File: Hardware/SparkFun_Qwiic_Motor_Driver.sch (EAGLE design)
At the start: 42 parts, among them U1 CY8C4245LQI-483, U2 DRV8835

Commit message: v01
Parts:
- LOGO3: value SFE_LOGO_NAME_FLAME.1_INCH -> SFE_LOGO_NAME.1_INCH; device SparkFun-Aesthetics:SFE_LOGO_NAME_FLAME.1_INCH -> SparkFun-Aesthetics:SFE_LOGO_NAME.1_INCH
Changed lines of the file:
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@@
 <part name="GND25" library="SparkFun-Aesthetics" deviceset="GND" device=""/>
 <part name="LOGO2" library="SparkFun-Aesthetics" deviceset="OSHW-LOGO" device="MINI"/>
-<part name="LOGO3" library="SparkFun-Aesthetics" deviceset="SFE_LOGO_NAME_FLAME" device=".1_INCH"/>
+<part name="LOGO3" library="SparkFun-Aesthetics" deviceset="SFE_LOGO_NAME" device=".1_INCH"/>
 <part name="R6" library="SparkFun-Resistors" deviceset="470OHM" device="-0603-1/10W-1%" value="470"/>
 <part name="GND26" library="SparkFun-Aesthetics" deviceset="GND" device=""/>

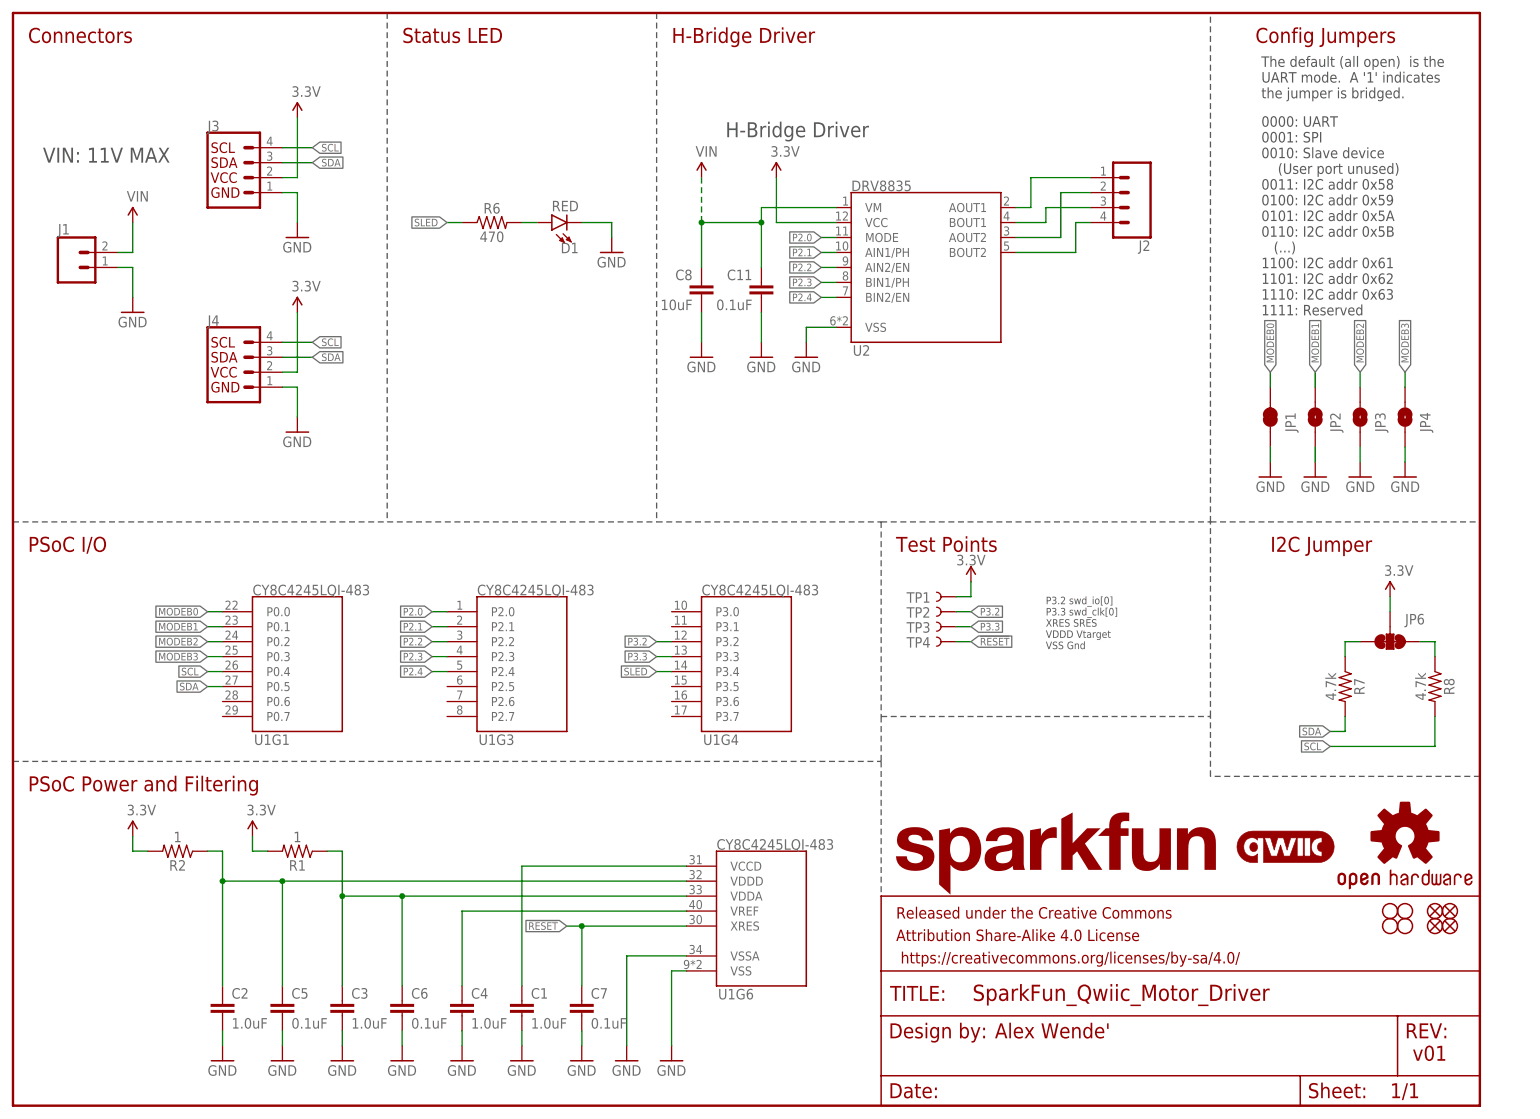
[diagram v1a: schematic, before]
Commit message: v01 Design Review Changes
- Added I2C test points
- Moved motor connector symbol to connection section
- Changed status LED to blue
- Adjusted VIN trace width
- Added SFE flame to top side of board
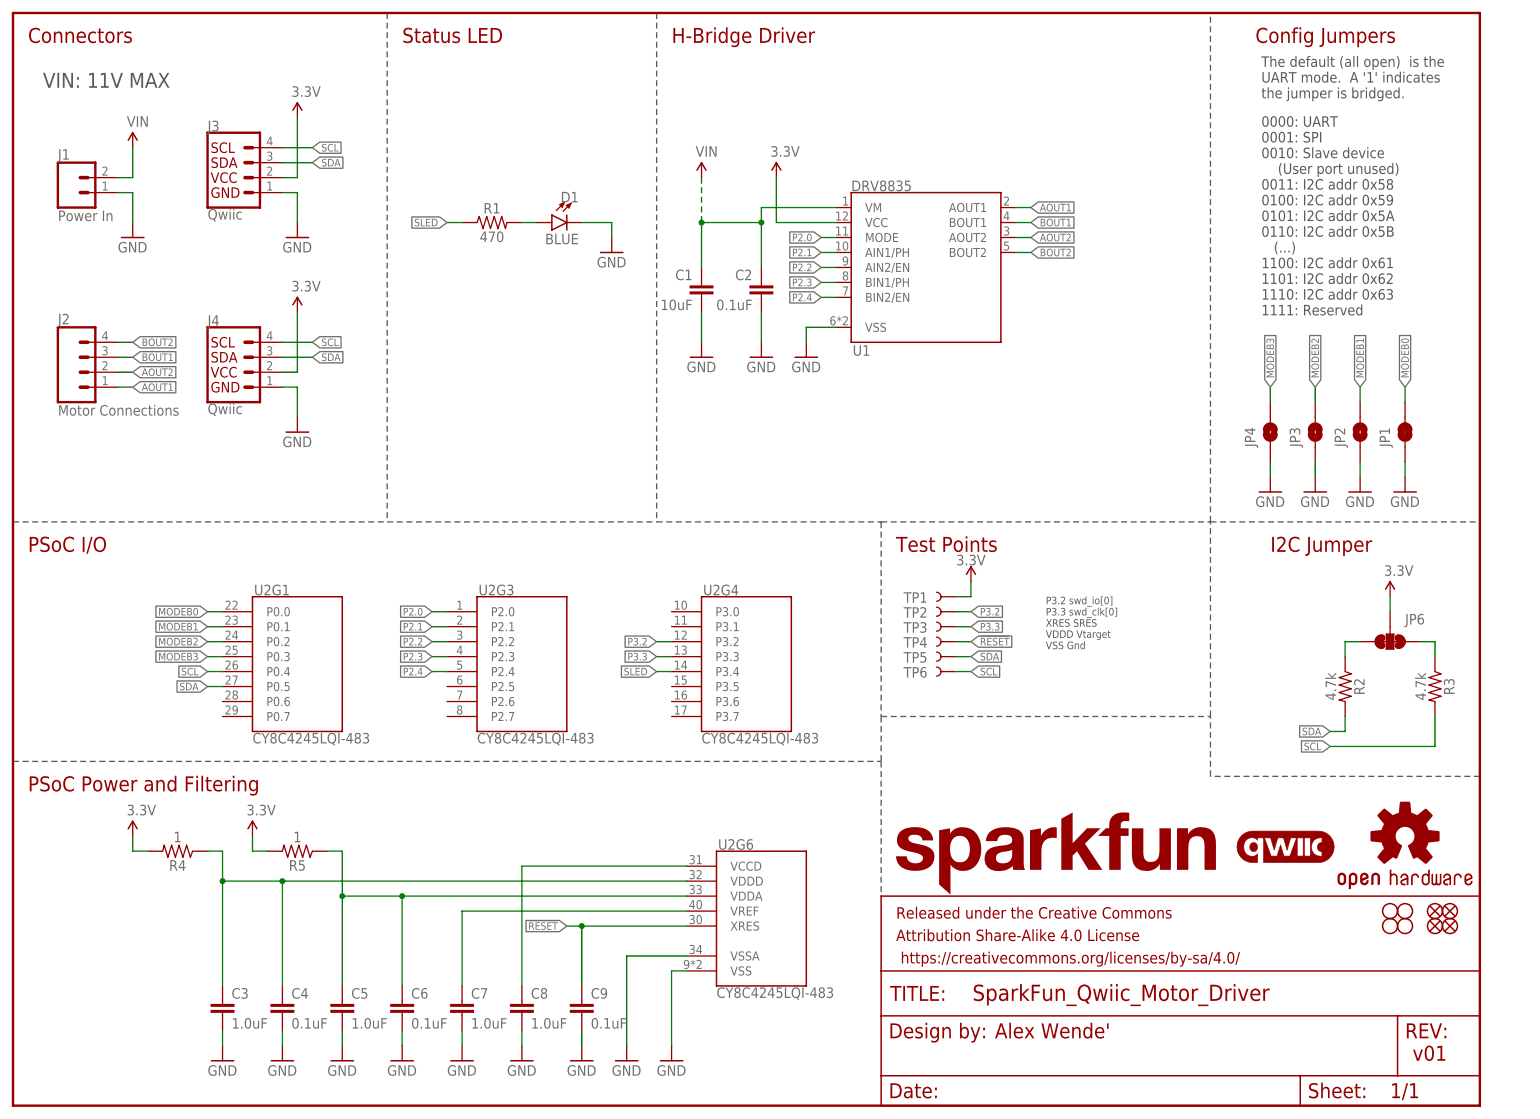
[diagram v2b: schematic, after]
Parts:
- removed C11: 0.1uF, SparkFun-Capacitors:0.1UF-0402-16V-10%
- removed R6: 470, SparkFun-Resistors:470OHM-0603-1/10W-1%
- removed R7: 4.7k, SparkFun-Resistors:4.7KOHM-0603-1/10W-1%
- added C9: 0.1uF, SparkFun-Capacitors:0.1UF-0402-16V-10%
- added R4, R5: 1, SparkFun-Resistors:1OHM-0603-1/10W-1%
- added TP5, TP6: TEST-POINTTP_15TH_THRU, SparkFun-Connectors:TEST-POINTTP_15TH_THRU
- C1: value 1.0uF -> 10uF; device SparkFun-Capacitors:1.0UF-0402-16V-10% -> SparkFun-Capacitors:10UF-0805-25V-10%
- C2, C4: value 1.0uF -> 0.1uF; device SparkFun-Capacitors:1.0UF-0402-16V-10% -> SparkFun-Capacitors:0.1UF-0402-16V-10%
- C5, C7: value 0.1uF -> 1.0uF; device SparkFun-Capacitors:0.1UF-0402-16V-10% -> SparkFun-Capacitors:1.0UF-0402-16V-10%
- C8: value 10uF -> 1.0uF; device SparkFun-Capacitors:10UF-0805-25V-10% -> SparkFun-Capacitors:1.0UF-0402-16V-10%
- D1: value RED -> BLUE; device SparkFun-LED:LED-RED0603 -> SparkFun-LED:LED-BLUE0603
- J1: value (none) -> Power In
- J2: value (none) -> Motor Connections
- J3, J4: value (none) -> Qwiic
- R1: value 1 -> 470; device SparkFun-Resistors:1OHM-0603-1/10W-1% -> SparkFun-Resistors:470OHM-0603-1/10W-1%
- R2: value 1 -> 4.7k; device SparkFun-Resistors:1OHM-0603-1/10W-1% -> SparkFun-Resistors:4.7KOHM-0603-1/10W-1%
- TP1, TP4: value RESET -> TEST-POINTTP_15TH_THRU
- TP2: value SWD_IO -> TEST-POINTTP_15TH_THRU
- TP3: value SWD_CLK -> TEST-POINTTP_15TH_THRU
- U1: value CY8C4245LQI-483 -> DRV8835; device PSOC4TempLib:CY8C4245LQI -> SparkFun-IC-Special-Function:DRV883X; PROD_ID (none) -> IC-13342
- U2: value DRV8835 -> CY8C4245LQI-483; device PSOC4TempLib:DRV883X -> SparkFun-IC-Microcontroller:PSOC4_4200_40QFN; PROD_ID IC-13342 -> (none)
- renumbered R8 to R3
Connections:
- net !RESET: now also C9.1, U2G6.XRES; no longer C7.1, U1G6.XRES
- net 3.3V: now also R4.2, R5.2, U1.VCC; no longer R1.2, R2.2, U2.VCC
- net AOUT1: now also U1.AOUT1; no longer U2.AOUT1
- net AOUT2: now also U1.AOUT2; no longer U2.AOUT2
- net BOUT1: now also U1.BOUT1; no longer U2.BOUT1
- net BOUT2: now also U1.BOUT2; no longer U2.BOUT2
- net GND: now also C9.2, U1.VSS, U2G6.VSS, U2G6.VSSA; no longer C11.2, U1G6.VSS, U1G6.VSSA, U2.VSS
- net MODEB0: now also U2G1.P0.0; no longer U1G1.P0.0
- net MODEB1: now also U2G1.P0.1; no longer U1G1.P0.1
- net MODEB2: now also U2G1.P0.2; no longer U1G1.P0.2
- net MODEB3: now also U2G1.P0.3; no longer U1G1.P0.3
- net N$1: now also C8.1, U2G6.VCCD; no longer C1.1, U1G6.VCCD
- net N$10: now also R1.2; no longer R6.2
- net N$12: now also R2.1; no longer R7.1
- net N$3: now also C5.1, R5.1, U2G6.VDDA; no longer C3.1, R1.1, U1G6.VDDA
- net N$4: now also C7.1, U2G6.VREF; no longer C4.1, U1G6.VREF
- net P2.0: now also U1.MODE, U2G3.P2.0; no longer U1G3.P2.0, U2.MODE
- net P2.1: now also U1.AIN1/PH, U2G3.P2.1; no longer U1G3.P2.1, U2.AIN1/PH
- net P2.2: now also U1.AIN2/EN, U2G3.P2.2; no longer U1G3.P2.2, U2.AIN2/EN
- net P2.3: now also U1.BIN1/PH, U2G3.P2.3; no longer U1G3.P2.3, U2.BIN1/PH
- net P2.4: now also U1.BIN2/EN, U2G3.P2.4; no longer U1G3.P2.4, U2.BIN2/EN
- net P3.2: now also U2G4.P3.2; no longer U1G4.P3.2
- net P3.3: now also U2G4.P3.3; no longer U1G4.P3.3
- net SCL: now also TP6.1, U2G1.P0.4; no longer U1G1.P0.4
- net SDA: now also R2.2, TP5.1, U2G1.P0.5; no longer R7.2, U1G1.P0.5
- net SLED: now also R1.1, U2G4.P3.4; no longer R6.1, U1G4.P3.4
- net VDDD: now also C3.1, C4.1, R4.1, U2G6.VDDD; no longer C2.1, C5.1, R2.1, U1G6.VDDD
- net VIN: now also C1.1, C2.1, U1.VM; no longer C11.1, C8.1, U2.VM
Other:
- moved on the sheet: C1, C2, C3, C4, C5, C7, C8, D1, J1, J2, JP1, JP2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

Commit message: v10
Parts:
- JP1: device SparkFun-Jumpers:JUMPER-SMT_2_NC_TRACE_NO-SILK -> SparkFun-Jumpers:JUMPER-SMT_2_NO_NO-SILK
- JP4: device SparkFun-Jumpers:JUMPER-SMT_2_NO_NO-SILK -> SparkFun-Jumpers:JUMPER-SMT_2_NC_TRACE_NO-SILK
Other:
- note added: "Alex Wende"
- note added: "P3.2 swd_io[0] P3.3 swd_clk[0]"
- note added: "v10"
- note removed: "Alex Wende'"
- note removed: "P3.2 swd_io[0] P3.3 swd_clk[0] XRES SRES VDDD Vtarget VSS Gnd"
- note removed: "v01"
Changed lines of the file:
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@@
 <part name="C2" library="SparkFun-Capacitors" deviceset="0.1UF" device="-0402-16V-10%" value="0.1uF"/>
 <part name="GND23" library="SparkFun-Aesthetics" deviceset="GND" device=""/>
-<part name="JP4" library="SparkFun-Jumpers" deviceset="JUMPER-SMT_2_NO" device="_NO-SILK" value="JUMPER-PAD-2"/>
+<part name="JP4" library="SparkFun-Jumpers" deviceset="JUMPER-SMT_2_NC_TRACE" device="_NO-SILK" value="JUMPER-PAD-2"/>
 <part name="JP3" library="SparkFun-Jumpers" deviceset="JUMPER-SMT_2_NO" device="_NO-SILK" value="JUMPER-PAD-2"/>
 <part name="JP2" library="SparkFun-Jumpers" deviceset="JUMPER-SMT_2_NO" device="_NO-SILK" value="JUMPER-PAD-2"/>
-<part name="JP1" library="SparkFun-Jumpers" deviceset="JUMPER-SMT_2_NC_TRACE" device="_NO-SILK" value="JUMPER-PAD-2"/>
+<part name="JP1" library="SparkFun-Jumpers" deviceset="JUMPER-SMT_2_NO" device="_NO-SILK" value="JUMPER-PAD-2"/>
 <part name="GND25" library="SparkFun-Aesthetics" deviceset="GND" device=""/>
 <part name="LOGO2" library="SparkFun-Aesthetics" deviceset="OSHW-LOGO" device="MINI"/>
@@
 <text x="2.54" y="53.34" size="2.54" layer="94" font="vector" ratio="15">PSoC Power and Filtering</text>
 <text x="210.82" y="180.34" size="2.54" layer="94" font="vector" ratio="15">Config Jumpers</text>
-<text x="166.624" y="11.43" size="2.54" layer="94" font="vector">Alex Wende'</text>
+<text x="166.624" y="11.43" size="2.54" layer="94" font="vector">Alex Wende</text>
 <text x="2.54" y="93.98" size="2.54" layer="94" font="vector" ratio="15">PSoC I/O</text>
-<text x="237.49" y="7.62" size="2.54" layer="94" font="vector">v01</text>
+<text x="237.49" y="7.62" size="2.54" layer="94" font="vector">v10</text>
 <text x="175.26" y="86.36" size="1.27" layer="97" font="vector" rot="MR180">P3.2 swd_io[0]
 P3.3 swd_clk[0]
-XRES SRES
-VDDD Vtarget
-VSS Gnd</text>
+</text>
 <text x="211.836" y="167.894" size="1.778" layer="97" font="vector" align="top-left">0000: UART
 0001: SPI

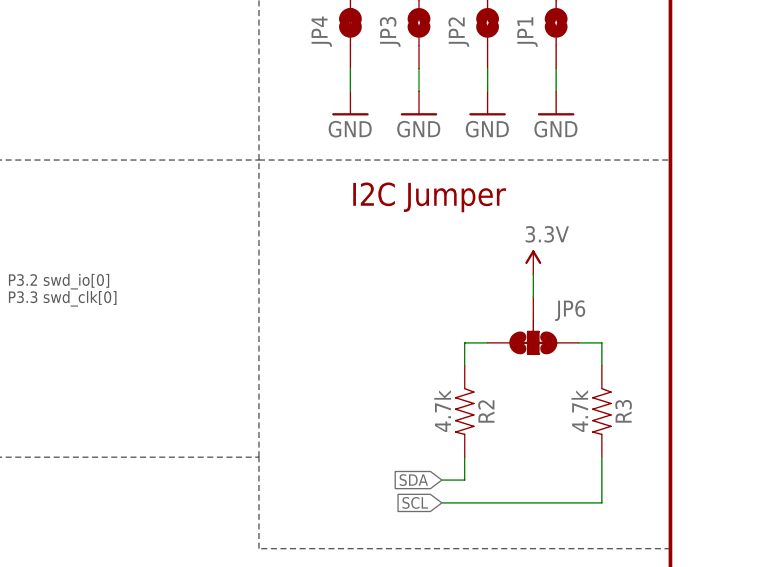
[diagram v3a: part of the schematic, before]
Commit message: v10 Update
- Added new 4-pin screw terminal instead of 2x2-pin screw terminals
- Added note about cutting traces to disable I2C pullup resistors
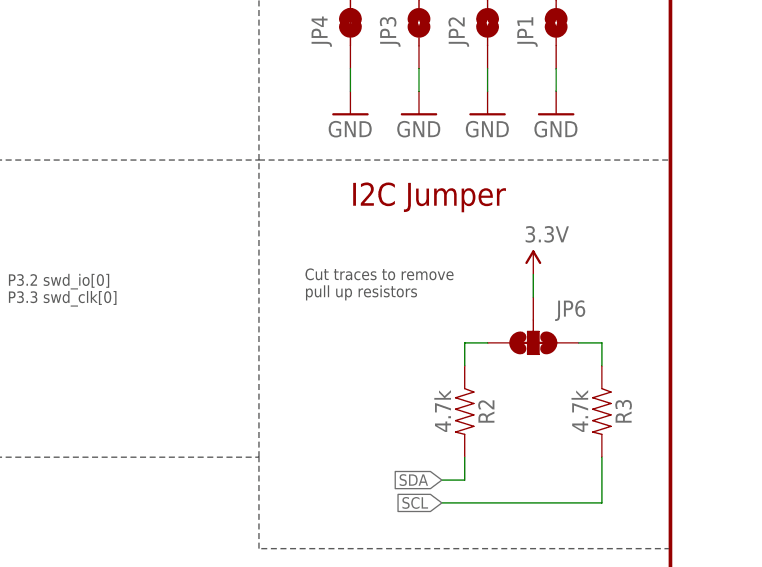
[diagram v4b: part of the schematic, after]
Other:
- note added: "Cut traces to remove pull up resistors"
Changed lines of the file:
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@@
 <wire x1="63.5" y1="185.42" x2="63.5" y2="99.06" width="0.1524" layer="97" style="shortdash"/>
 <text x="5.08" y="172.72" size="2.54" layer="97" font="vector" ratio="15">VIN: 11V MAX</text>
+<text x="208.28" y="83.82" size="1.27" layer="97" font="vector">Cut traces to remove
+pull up resistors</text>
 </plain>
 <instances>
